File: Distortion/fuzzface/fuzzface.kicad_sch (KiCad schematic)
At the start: 13 parts, among them J1 Conn_01x04_Female, Q1 AC128, Q2 AC128

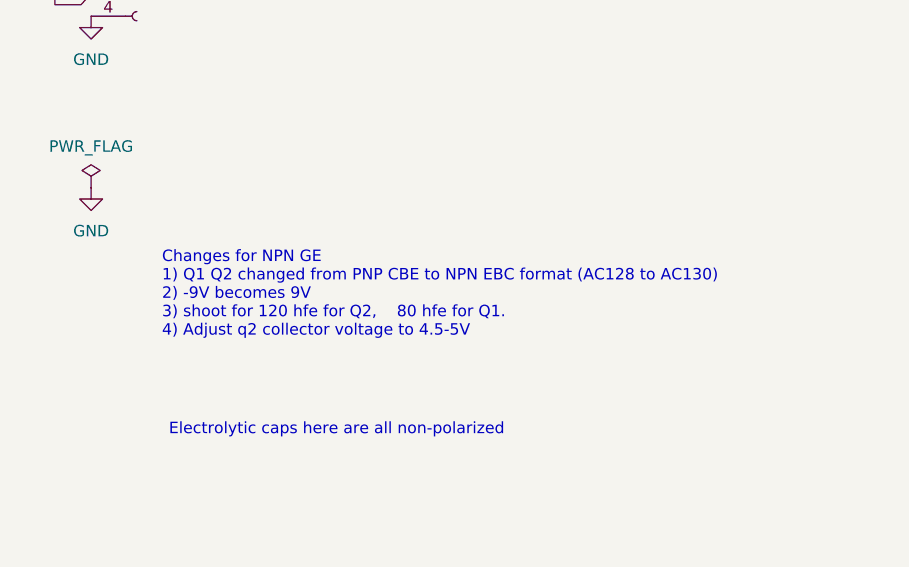
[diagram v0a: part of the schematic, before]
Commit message: added engineers thumb, ramshead-bmp
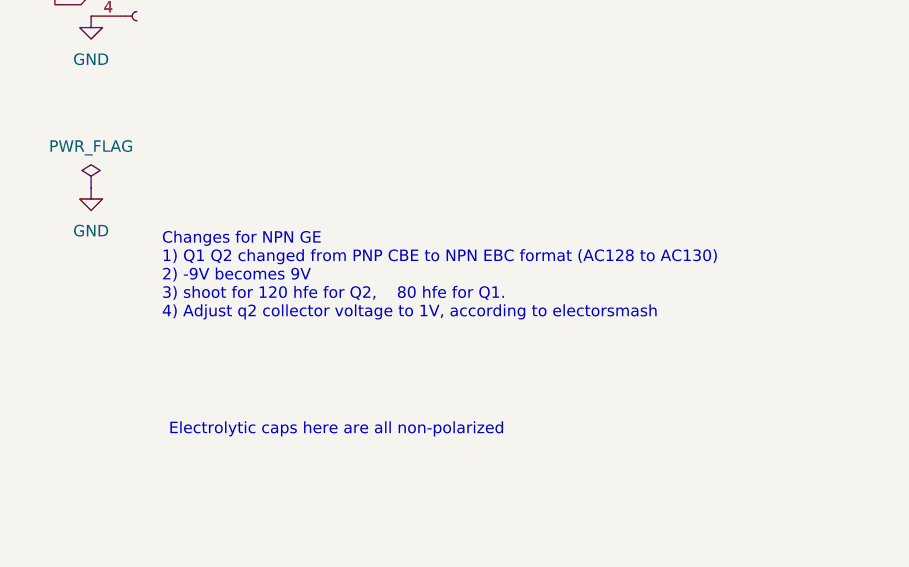
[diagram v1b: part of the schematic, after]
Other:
- note added: "Changes for NPN GE 1) Q1 Q2 changed from PNP CBE to NPN EBC format (AC128 to AC130) 2) -9V becomes 9V 3) shoot for 120 hfe for Q2, 80 hfe for Q1. 4) Adjust q2 collector voltage to 1V, according to electorsmash"
- note removed: "Changes for NPN GE 1) Q1 Q2 changed from PNP CBE to NPN EBC format (AC128 to AC130) 2) -9V becomes 9V 3) shoot for 120 hfe for Q2, 80 hfe for Q1. 4) Adjust q2 collector voltage to 4.5-5V"
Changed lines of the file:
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@@
     (effects (font (size 1.27 1.27)) (justify left bottom))
   )
-  (text "Changes for NPN GE\n1) Q1 Q2 changed from PNP CBE to NPN EBC format (AC128 to AC130)\n2) -9V becomes 9V\n3) shoot for 120 hfe for Q2,    80 hfe for Q1.\n4) Adjust q2 collector voltage to 4.5-5V\n\n\n"
+  (text "Changes for NPN GE\n1) Q1 Q2 changed from PNP CBE to NPN EBC format (AC128 to AC130)\n2) -9V becomes 9V\n3) shoot for 120 hfe for Q2,    80 hfe for Q1.\n4) Adjust q2 collector voltage to 1V, according to electorsmash\n\n\n\n"
     (at 168.656 77.47 0)
     (effects (font (size 1.27 1.27)) (justify left bottom))

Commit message: added ejfuzzface
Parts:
- C3: footprint Capacitor_THT:C_Radial_D10.0mm_H12.5mm_P5.00mm -> Capacitor_THT:C_Radial_D6.3mm_H7.0mm_P2.50mm
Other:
- note added: "Electrolytic caps here are all non-polarized If using polarized caps, and -9v with PNP germanium, GND is the positive side and the input 2.2u cap is positive towards in. user1 layer has the + side denoted."
- note removed: "Electrolytic caps here are all non-polarized"
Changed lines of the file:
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@@
     (stroke (width 0) (type default))
   )
-  (text "Electrolytic caps here are all non-polarized\n" (at 169.418 84.328 0)
+  (text "Electrolytic caps here are all non-polarized\nIf using polarized caps, and -9v with PNP germanium, GND is the positive side\nand the input 2.2u cap is positive towards in.\nuser1 layer has the + side denoted.  \n"
+    (at 169.418 84.328 0)
     (effects (font (size 1.27 1.27)) (justify left bottom))
   )
@@
       (effects (font (size 1.27 1.27)) (justify left))
     )
-    (property "Footprint" "Capacitor_THT:C_Radial_D10.0mm_H12.5mm_P5.00mm" (at 73.3552 36.322 0)
-      (effects (font (size 1.27 1.27)) hide)
-    )
+    (property "Footprint" "Capacitor_THT:C_Radial_D6.3mm_H7.0mm_P2.50mm" (at 73.3552 36.322 0)
+      (effects (font (size 1.27 1.27)) hide)
+    )
